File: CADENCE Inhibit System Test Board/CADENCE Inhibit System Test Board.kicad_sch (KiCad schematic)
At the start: 70 parts, among them IC1 LTC7004IMSE#WTRPBF, IC2 LTC7004IMSE#WTRPBF, IC3 LTC7004IMSE#WTRPBF, IC4 LTC7004IMSE#WTRPBF, IC5 LTC7004IMSE#WTRPBF, J1 INHIBIT_P2, J10 Conn_01x04, J11 Conn_01x02, J2 INHIBIT_P2, J3 INHIBIT_P2, J4 INHIBIT_P2, J5 INHIBIT_P2, J6 INHIBIT_P2, J7 INHIBIT_P2, J8 INHIBIT_P2, J9 INHIBIT_P2, Q1 SUD23N06-31-GE3, Q2 SUD23N06-31-GE3, Q3 SUD23N06-31-GE3, Q4 SUD23N06-31-GE3, Q5 SUD23N06-31-GE3, Q6 SUD23N06-31-GE3, Q7 SUD23N06-31-GE3, SW1 SW_SPST, SW2 SW_SPST, SW3 SW_SPST, SW4 SW_SPDT, SW5 SW_SPST, SW6 SW_SPST, SW7 SW_SPST, SW8 SW_SPST, SW9 SW_SPST, U1 MIC4427YM-TR, U2 MIC4427YM-TR

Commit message: added footprints to testpoints
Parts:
- TP4, TP6, TP7: footprint (none) -> TestPoint:TestPoint_THTPad_D1.0mm_Drill0.5mm
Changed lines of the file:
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@@
 			)
 		)
-		(property "Footprint" ""
+		(property "Footprint" "TestPoint:TestPoint_THTPad_D1.0mm_Drill0.5mm"
 			(at 73.66 46.99 0)
 			(hide yes)
@@
 			)
 		)
-		(property "Footprint" ""
+		(property "Footprint" "TestPoint:TestPoint_THTPad_D1.0mm_Drill0.5mm"
 			(at 115.57 109.22 0)
 			(hide yes)
@@
 			)
 		)
-		(property "Footprint" ""
+		(property "Footprint" "TestPoint:TestPoint_THTPad_D1.0mm_Drill0.5mm"
 			(at 115.57 170.18 0)
 			(hide yes)

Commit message: pcb layout
confident in completion of IC3, IC4, IC1, foot switches, and low power side
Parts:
- TP5, TP8, TP9: footprint (none) -> TestPoint:TestPoint_THTPad_D1.0mm_Drill0.5mm
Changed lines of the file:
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@@
 			)
 		)
-		(property "Footprint" ""
+		(property "Footprint" "TestPoint:TestPoint_THTPad_D1.0mm_Drill0.5mm"
 			(at 224.79 34.29 0)
 			(hide yes)
@@
 			)
 		)
-		(property "Footprint" ""
+		(property "Footprint" "TestPoint:TestPoint_THTPad_D1.0mm_Drill0.5mm"
 			(at 232.41 207.01 0)
 			(hide yes)
@@
 			)
 		)
-		(property "Footprint" ""
+		(property "Footprint" "TestPoint:TestPoint_THTPad_D1.0mm_Drill0.5mm"
 			(at 224.79 105.41 0)
 			(hide yes)

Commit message: tracing more
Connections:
- net Cell 1+: now also Q3.1 (S); no longer Q3.3 (D)
- net at C6.1, IC1.8 (TS), Q6.3 (D)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: now also Q3.3 (D); no longer Q3.1 (S)
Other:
- moved on the sheet: Q3
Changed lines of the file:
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@@
 	(symbol
 		(lib_id "Transistor_FET:Q_NMOS_SGD")
-		(at 215.9 110.49 90)
+		(at 215.9 110.49 270)
+		(mirror x)
 		(unit 1)
 		(body_style 1)
@@
 		(in_pos_files yes)
 		(dnp no)
-		(fields_autoplaced yes)
 		(property "Reference" "Q3"
 			(at 215.9 101.6 90)
@@
 		)
 		(property "Footprint" "Package_TO_SOT_SMD:TO-252-2"
-			(at 213.36 105.41 0)
+			(at 218.44 105.41 0)
 			(hide yes)
 			(show_name no)
@@
 		)
 		(property "Value" "VSS"
-			(at 191.77 66.548 0)
+			(at 192.278 66.04 0)
 			(show_name no)
 			(do_not_autoplace no)

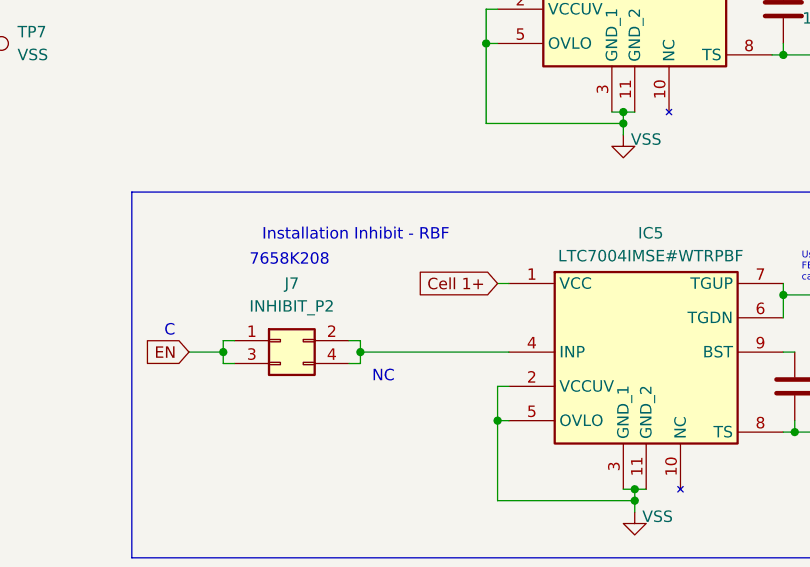
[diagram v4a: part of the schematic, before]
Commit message: Continued adding traces for gnd
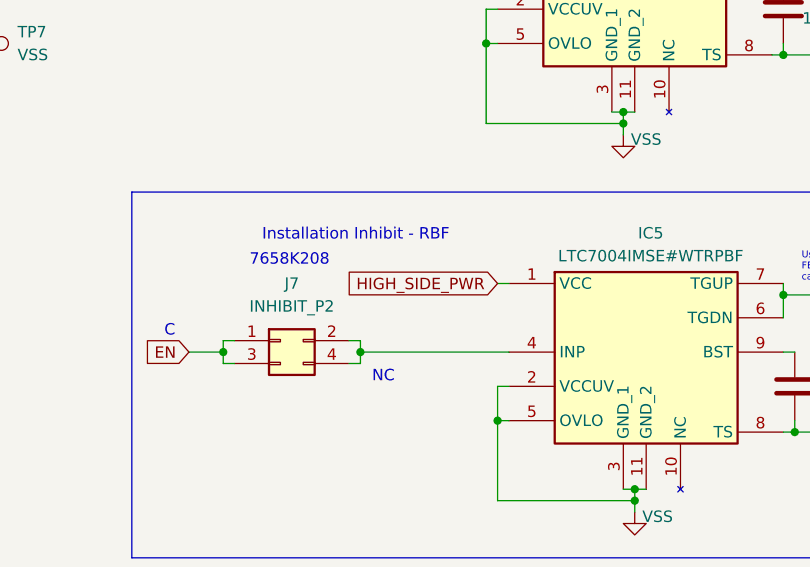
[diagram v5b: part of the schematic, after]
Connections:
- net Cell 1+: no longer IC5.1 (VCC)
- net HIGH_SIDE_PWR: now also IC5.1 (VCC)
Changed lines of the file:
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@@
 		)
 	)
-	(global_label "Cell 1+"
+	(global_label "HIGH_SIDE_PWR"
 		(shape input)
 		(at 173.99 191.77 180)
@@
 		)
 		(property "Intersheetrefs" "${INTERSHEET_REFS}"
-			(at 163.5663 191.77 0)
+			(at 156.3091 191.77 0)
 			(hide yes)
 			(show_name no)
